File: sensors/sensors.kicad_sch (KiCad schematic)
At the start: 6 parts, among them J1 Conn 1x3, U1 TCRT5000

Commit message: Changed the layout of the files
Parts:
- removed H2: MountingHole, MountingHole:MountingHole_3.2mm_M3, symbol Mechanical:MountingHole
- added TP1: TestPoint, TestPoint:TestPoint_Plated_Hole_D2.0mm, symbol Connector:TestPoint
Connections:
- net Vout: now also TP1.1
- no-connect marks 2 -> 1
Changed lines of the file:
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@@
 	(generator_version "9.0")
 	(paper "A4")
+	(junction
+		(at 95.25 87.63)
+		(diameter 0)
+		(color 0 0 0 0)
+	)
 	(no_connect
 		(at 50.8 44.45)
-	)
-	(no_connect
-		(at 50.8 114.3)
 	)
 	(wire
@@
 	)
 	(symbol
-		(lib_id "Mechanical:MountingHole")
-		(at 50.8 114.3 0)
-		(unit 1)
-		(exclude_from_sim no)
-		(in_bom no)
-		(on_board yes)
-		(dnp no)
-		(fields_autoplaced yes)
-		(property "Reference" "H2"
-			(at 53.34 113.0299 0)
-			(effects
-				(font
-					(size 1.27 1.27)
-				)
-				(justify left)
-			)
-		)
-		(property "Value" "MountingHole"
-			(at 53.34 115.5699 0)
-			(effects
-				(font
-					(size 1.27 1.27)
-				)
-				(justify left)
-			)
-		)
-		(property "Footprint" "MountingHole:MountingHole_3.2mm_M3"
-			(at 50.8 114.3 0)
-			(effects
-				(font
-					(size 1.27 1.27)
-				)
-				(hide yes)
-			)
-		)
-		(property "Datasheet" "~"
-			(at 50.8 114.3 0)
-			(effects
-				(font
-					(size 1.27 1.27)
-				)
-				(hide yes)
-			)
-		)
-		(property "Description" "Mounting Hole without connection"
-			(at 50.8 114.3 0)
-			(effects
-				(font
-					(size 1.27 1.27)
-				)
-				(hide yes)
-			)
-		)
-		(instances
-			(project ""
-				(path "/7a5c889d-d948-4110-bf7e-4c334aa2755f"
-					(reference "H2")
-					(unit 1)
-				)
-			)
-		)
-	)
-	(symbol
 		(lib_id "lib:TCRT5000")
 		(at 95.25 80.01 0)
@@
 					(unit 1)
 				)
+			)
+		)
+	)
+	(symbol
+		(lib_id "Connector:TestPoint")
+		(at 95.25 87.63 0)
+		(unit 1)
+		(exclude_from_sim no)
+		(in_bom yes)
+		(on_board yes)
+		(dnp no)
+		(fields_autoplaced yes)
+		(property "Reference" "TP1"
+			(at 97.79 83.0579 0)
+			(effects
+				(font
+					(size 1.27 1.27)
+				)
+				(justify left)
+			)
+		)
+		(property "Value" "TestPoint"
+			(at 97.79 85.5979 0)
+			(effects
+				(font
+					(size 1.27 1.27)
+				)
+				(justify left)
+			)
+		)
+		(property "Footprint" "TestPoint:TestPoint_Plated_Hole_D2.0mm"
+			(at 100.33 87.63 0)
+			(effects
+				(font
+					(size 1.27 1.27)
+				)
+				(hide yes)
+			)
+		)
+		(property "Datasheet" "~"
+			(at 100.33 87.63 0)
+			(effects
+				(font
+					(size 1.27 1.27)
+				)
+				(hide yes)
+			)
+		)
+		(property "Description" "test point"
+			(at 95.25 87.63 0)
+			(effects
+				(font
+					(size 1.27 1.27)
+				)
+				(hide yes)
+			)
+		)
+		(pin "1"
+		)
+		(instances
+			(project ""
+				(path "/7a5c889d-d948-4110-bf7e-4c334aa2755f"
+					(reference "TP1")
+					(unit 1)
+				)

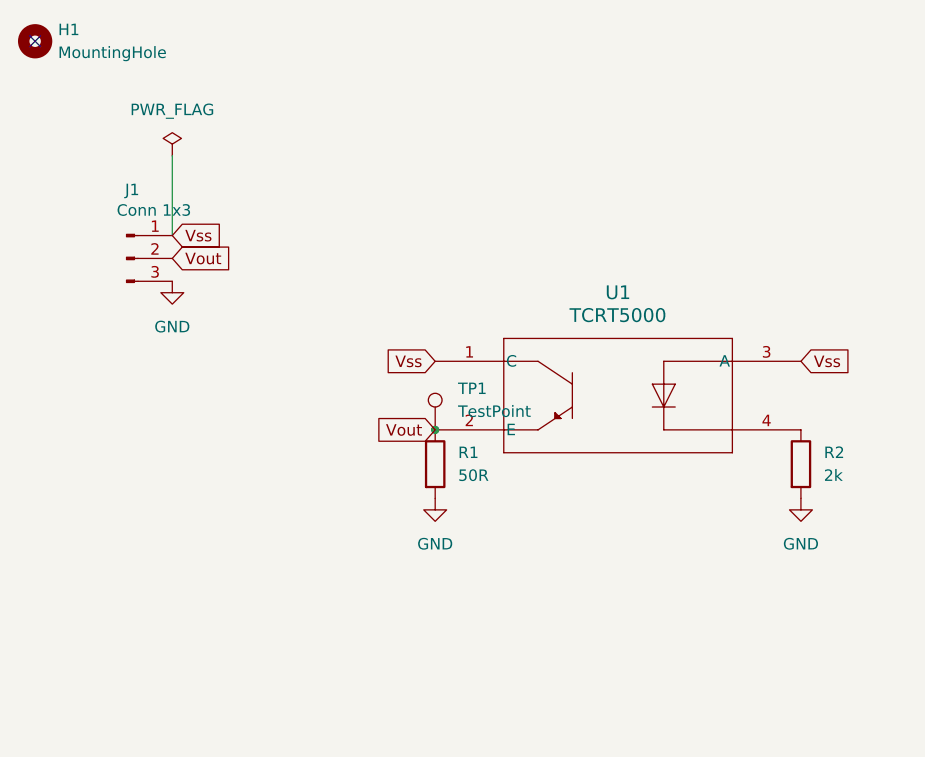
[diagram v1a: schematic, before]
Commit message: Added a potentiometer to the sensor board.
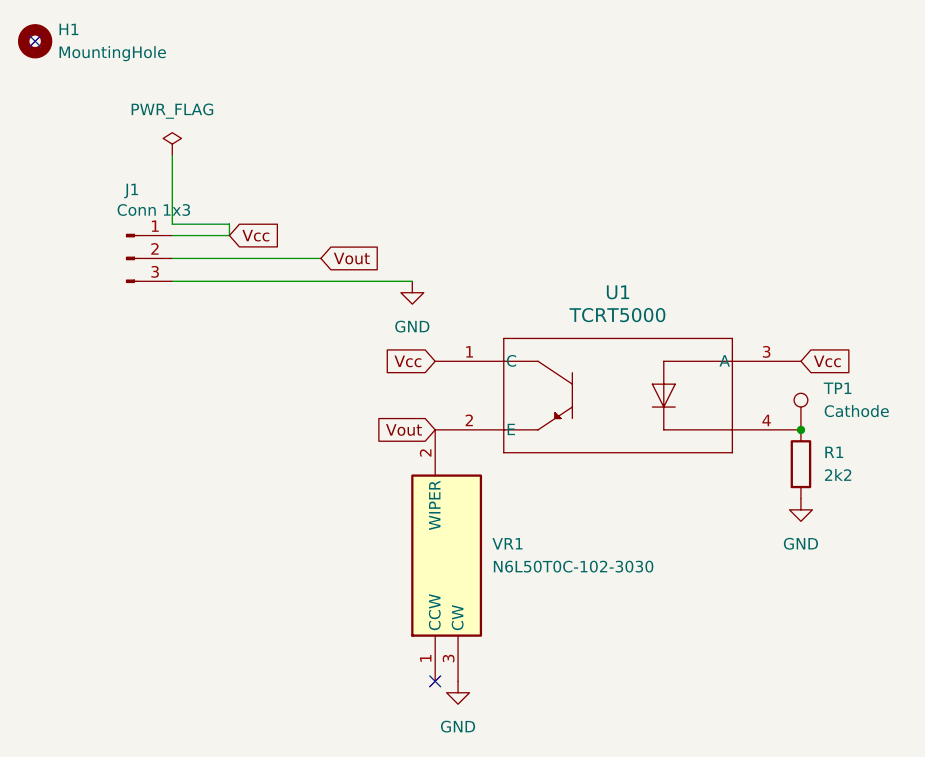
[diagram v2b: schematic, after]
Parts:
- removed R2: 2k, Resistor_THT:R_Axial_DIN0207_L6.3mm_D2.5mm_P7.62mm_Horizontal, symbol Device:R
- added VR1: N6L50T0C-102-3030, N6L50T0C-103-3030:N6L50T0C1033030, symbol N6L50T0C-103-3030:N6L50T0C-103-3030
- R1: value 50R -> 2k2; footprint Resistor_THT:R_Axial_DIN0207_L6.3mm_D2.5mm_P7.62mm_Horizontal -> Resistor_SMD:R_0805_2012Metric_Pad1.20x1.40mm_HandSolder
- TP1: value TestPoint -> Cathode
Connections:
- net GND: now also VR1.3 (CW)
- net Vout: now also VR1.2 (WIPER); no longer R1.1, TP1.1
- net at U1.4: now also R1.1, TP1.1
- net Vss renamed Vcc
- no-connect marks 1 -> 2
